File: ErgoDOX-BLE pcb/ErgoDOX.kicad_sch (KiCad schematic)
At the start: 116 parts, among them J1 Conn_01x04, J2 Conn_01x02_Female, J4 Conn_01x02, J5 Conn_01x02, J6 6PIN, P1 USB_C_Plug_USB2.0, Q1 Q_NPN_BCE, SW0:10 SW0:3, SW0:11 SW0:2, SW0:12 SW0:1, SW0:7 SW0:6, SW0:8 SW0:5, SW0:9 SW0:4, SW1:10 SW1:3, SW1:11 SW1:2, SW1:12 SW1:1, SW1:13 SW1:0, SW1:9 SW1:4, SW2:10 SW2:3, SW2:11 SW2:2, SW2:12 SW2:1, SW2:13 SW2:0, SW2:7 SW2:6, SW2:8 SW2:5, SW2:9 SW2:4, SW3:10 SW3:3, SW3:11 SW3:2, SW3:12 SW3:1, SW3:13 SW3:0, SW3:8 SW3:5, SW3:9 SW3:4, SW4:10 SW4:3, SW4:11 SW4:2, SW4:12 SW4:1, SW4:13 SW4:0, SW4:7 SW4:6, SW4:8 SW4:5, SW4:9 SW4:4, SW5:10 SW5:3, SW5:11 SW5:2, SW5:12 SW5:1, SW5:13 SW5:0, SW5:7 SW5:6, SW5:8 SW5:5, SW5:9 SW5:4, U1 MCP23018, U2 MCP73831-2-OT, U3 SPX3819M5-L-3-3

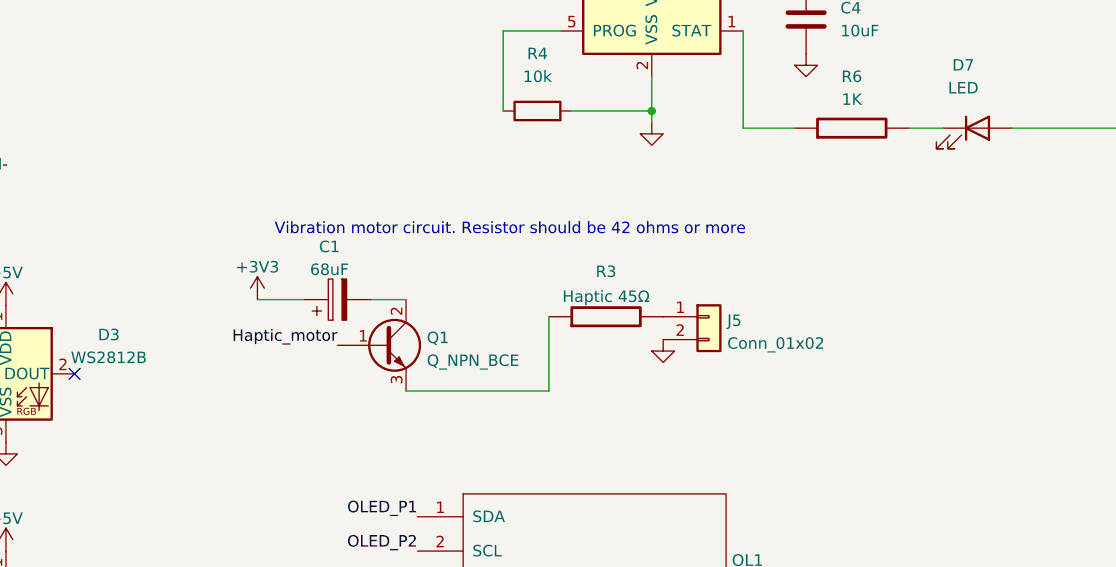
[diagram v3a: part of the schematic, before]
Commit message: Fixing some silk and moving components
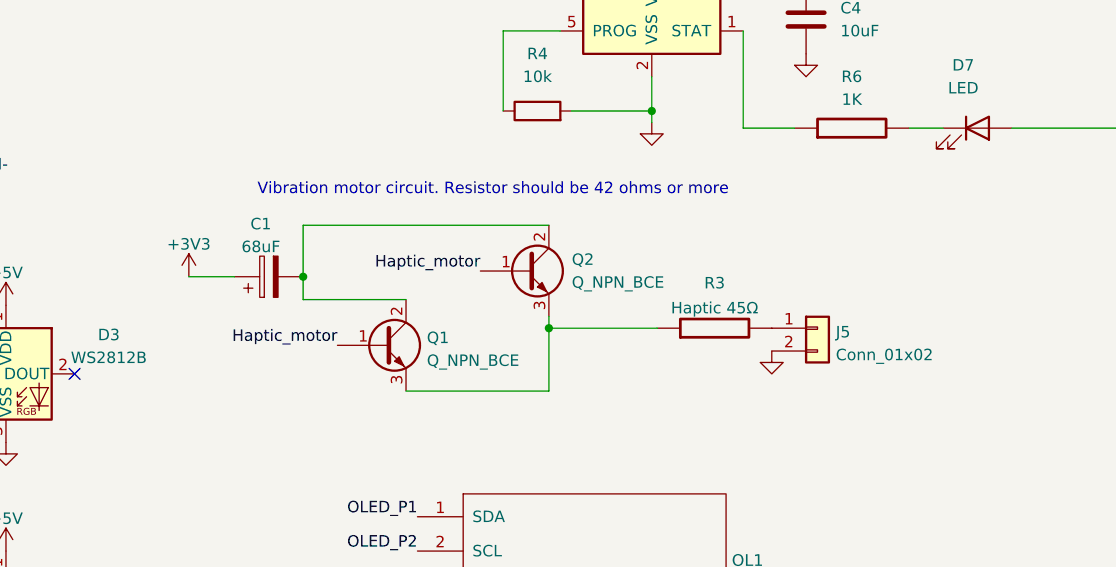
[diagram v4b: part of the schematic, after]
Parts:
- added Q2: Q_NPN_BCE, Package_TO_SOT_SMD:SOT-23, symbol Device:Q_NPN_BCE
- Q1: manf# (none) -> MMBT4401-TP
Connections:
- net Haptic_motor: now also Q2.1 (B)
- net at C1.2, Q1.2 (C): now also Q2.2 (C)
- net at Q1.3 (E), R3.1: now also Q2.3 (E)
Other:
- moved on the sheet: C1, J5, R3
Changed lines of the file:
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@@
   (junction (at 58.42 229.87) (diameter 0) (color 0 0 0 0)
   )
+  (junction (at 302.895 186.055) (diameter 0) (color 0 0 0 0)
+  )
   (junction (at 132.08 238.76) (diameter 0) (color 0 0 0 0)
   )
@@
   (junction (at 96.52 222.25) (diameter 0) (color 0 0 0 0)
   )
+  (junction (at 330.2 191.77) (diameter 0) (color 0 0 0 0)
+  )
   (junction (at 111.76 213.36) (diameter 0) (color 0 0 0 0)
   )
@@
     (stroke (width 0) (type default) (color 0 0 0 0))
   )
-  (wire (pts (xy 330.2 198.755) (xy 330.2 190.5))
+  (wire (pts (xy 330.2 198.755) (xy 330.2 191.77))
     (stroke (width 0) (type default) (color 0 0 0 0))
   )
@@
     (stroke (width 0) (type default) (color 0 0 0 0))
   )
+  (wire (pts (xy 330.2 191.77) (xy 330.2 190.5))
+    (stroke (width 0) (type default) (color 0 0 0 0))
+  )
   (wire (pts (xy 93.98 147.32) (xy 111.76 147.32))
     (stroke (width 0) (type default) (color 0 0 0 0))
@@
     (stroke (width 0) (type default) (color 0 0 0 0))
   )
+  (wire (pts (xy 330.2 191.77) (xy 342.265 191.77))
+    (stroke (width 0) (type default) (color 0 0 0 0))
+  )
   (wire (pts (xy 93.98 229.87) (xy 93.98 234.95))
     (stroke (width 0) (type default) (color 0 0 0 0))
@@
     (stroke (width 0) (type default) (color 0 0 0 0))
   )
-  (wire (pts (xy 297.815 188.595) (xy 302.895 188.595))
+  (wire (pts (xy 290.195 186.055) (xy 295.275 186.055))
     (stroke (width 0) (type default) (color 0 0 0 0))
   )
@@
     (stroke (width 0) (type default) (color 0 0 0 0))
   )
-  (wire (pts (xy 310.515 188.595) (xy 314.325 188.595))
+  (wire (pts (xy 302.895 188.595) (xy 314.325 188.595))
     (stroke (width 0) (type default) (color 0 0 0 0))
   )
@@
     (stroke (width 0) (type default) (color 0 0 0 0))
   )
+  (wire (pts (xy 302.895 180.34) (xy 330.2 180.34))
+    (stroke (width 0) (type default) (color 0 0 0 0))
+  )
   (wire (pts (xy 58.42 180.34) (xy 76.2 180.34))
     (stroke (width 0) (type default) (color 0 0 0 0))
@@
     (stroke (width 0) (type default) (color 0 0 0 0))
   )
+  (wire (pts (xy 302.895 186.055) (xy 302.895 180.34))
+    (stroke (width 0) (type default) (color 0 0 0 0))
+  )
   (wire (pts (xy 93.98 50.8) (xy 93.98 72.39))
     (stroke (width 0) (type default) (color 0 0 0 0))
@@
     (stroke (width 0) (type default) (color 0 0 0 0))
   )
+  (wire (pts (xy 302.895 188.595) (xy 302.895 186.055))
+    (stroke (width 0) (type default) (color 0 0 0 0))
+  )
   (wire (pts (xy 341.63 146.05) (xy 341.63 148.59))
     (stroke (width 0) (type default) (color 0 0 0 0))
@@
   )
   (text "Vibration motor circuit. Resistor should be 42 ohms or more"
-    (at 299.72 181.61 0)
+    (at 297.815 177.165 0)
     (effects (font (size 1.27 1.27)) (justify left bottom))
   )
@@
     (effects (font (size 1.27 1.27)) (justify right bottom))
   )
+  (label "Haptic_motor" (at 322.58 185.42 180)
+    (effects (font (size 1.27 1.27)) (justify right bottom))
+  )
   (label "D_IN_RIGHT+" (at 47.625 100.965 0)
     (effects (font (size 1.27 1.27)) (justify left bottom))
@@
     (pin "1")
   )
-  (symbol (lib_id "Device:C_Polarized") (at 306.705 188.595 90) (unit 1)
+  (symbol (lib_id "Device:C_Polarized") (at 299.085 186.055 90) (unit 1)
     (in_bom yes) (on_board yes) (fields_autoplaced)
-    (property "Reference" "C1" (id 0) (at 305.816 182.7362 90))
-    (property "Value" "68uF" (id 1) (at 305.816 185.2731 90))
-    (property "Footprint" "Capacitor_THT:CP_Radial_Tantal_D5.0mm_P5.00mm" (id 2) (at 310.515 187.6298 0)
+    (property "Reference" "C1" (id 0) (at 298.196 180.1962 90))
+    (property "Value" "68uF" (id 1) (at 298.196 182.7331 90))
+    (property "Footprint" "Capacitor_THT:CP_Radial_Tantal_D5.0mm_P5.00mm" (id 2) (at 302.895 185.0898 0)
       (effects (font (size 1.27 1.27)) hide)
     )
-    (property "Datasheet" "~" (id 3) (at 306.705 188.595 0)
+    (property "Datasheet" "~" (id 3) (at 299.085 186.055 0)
       (effects (font (size 1.27 1.27)) hide)
     )
@@
       (effects (font (size 1.27 1.27)) hide)
     )
+    (property "manf#" "MMBT4401-TP" (id 4) (at 311.785 193.675 0)
+      (effects (font (size 0 0)) hide)
+    )
     (pin "1")
     (pin "2")
@@
     (pin "1")
   )
+  (symbol (lib_id "Device:Q_NPN_BCE") (at 327.66 185.42 0) (unit 1)
+    (in_bom yes) (on_board yes) (fields_autoplaced)
+    (property "Reference" "Q2" (id 0) (at 332.74 184.1499 0)
+      (effects (font (size 1.27 1.27)) (justify left))
+    )
+    (property "Value" "Q_NPN_BCE" (id 1) (at 332.74 186.6899 0)
+      (effects (font (size 1.27 1.27)) (justify left))
+    )
+    (property "Footprint" "Package_TO_SOT_SMD:SOT-23" (id 2) (at 332.74 182.88 0)
+      (effects (font (size 1.27 1.27)) hide)
+    )
+    (property "Datasheet" "~" (id 3) (at 327.66 185.42 0)
+      (effects (font (size 1.27 1.27)) hide)
+    )
+    (property "manf#" "MMBT4401-TP" (id 4) (at 327.66 185.42 0)
+      (effects (font (size 1.27 1.27)) hide)
+    )
+    (pin "1")
+    (pin "2")
+    (pin "3")
+  )
   (symbol (lib_id "component:GND") (at 313.055 247.65 90) (unit 1)
     (in_bom yes) (on_board yes) (fields_autoplaced)
@@
     (pin "1")
   )
-  (symbol (lib_id "component:GND") (at 342.9 194.31 0) (unit 1)
+  (symbol (lib_id "component:GND") (at 354.965 195.58 0) (unit 1)
     (in_bom yes) (on_board yes) (fields_autoplaced)
-    (property "Reference" "#PWR032" (id 0) (at 342.9 194.31 0)
+    (property "Reference" "#PWR032" (id 0) (at 354.965 195.58 0)
       (effects (font (size 0.762 0.762)) hide)
     )
-    (property "Value" "GND" (id 1) (at 342.9 196.088 0)
+    (property "Value" "GND" (id 1) (at 354.965 197.358 0)
       (effects (font (size 0.762 0.762)) hide)
     )
-    (property "Footprint" "" (id 2) (at 342.9 194.31 0)
+    (property "Footprint" "" (id 2) (at 354.965 195.58 0)
       (effects (font (size 1.27 1.27)) hide)
     )
-    (property "Datasheet" "" (id 3) (at 342.9 194.31 0)
+    (property "Datasheet" "" (id 3) (at 354.965 195.58 0)
       (effects (font (size 1.27 1.27)) hide)
     )
@@
     (pin "4")
   )
-  (symbol (lib_id "power:+3V3") (at 297.815 188.595 0) (unit 1)
+  (symbol (lib_id "power:+3V3") (at 290.195 186.055 0) (unit 1)
     (in_bom yes) (on_board yes) (fields_autoplaced)
-    (property "Reference" "#PWR017" (id 0) (at 297.815 192.405 0)
+    (property "Reference" "#PWR017" (id 0) (at 290.195 189.865 0)
       (effects (font (size 1.27 1.27)) hide)
     )
-    (property "Value" "+3V3" (id 1) (at 297.815 184.9905 0))
-    (property "Footprint" "" (id 2) (at 297.815 188.595 0)
+    (property "Value" "+3V3" (id 1) (at 290.195 182.4505 0))
+    (property "Footprint" "" (id 2) (at 290.195 186.055 0)
       (effects (font (size 1.27 1.27)) hide)
     )
-    (property "Datasheet" "" (id 3) (at 297.815 188.595 0)
+    (property "Datasheet" "" (id 3) (at 290.195 186.055 0)
       (effects (font (size 1.27 1.27)) hide)
     )
@@
     (pin "6")
   )
-  (symbol (lib_id "Connector_Generic:Conn_01x02") (at 347.98 190.5 0) (unit 1)
+  (symbol (lib_id "Connector_Generic:Conn_01x02") (at 360.045 191.77 0) (unit 1)
     (in_bom yes) (on_board yes) (fields_autoplaced)
-    (property "Reference" "J5" (id 0) (at 350.012 190.9353 0)
+    (property "Reference" "J5" (id 0) (at 362.077 192.2053 0)
       (effects (font (size 1.27 1.27)) (justify left))
     )
-    (property "Value" "Conn_01x02" (id 1) (at 350.012 193.4722 0)
+    (property "Value" "Conn_01x02" (id 1) (at 362.077 194.7422 0)
       (effects (font (size 1.27 1.27)) (justify left))
     )
-    (property "Footprint" "Connector_PinHeader_2.00mm:PinHeader_1x02_P2.00mm_Vertical" (id 2) (at 347.98 190.5 0)
+    (property "Footprint" "Connector_PinHeader_2.00mm:PinHeader_1x02_P2.00mm_Vertical" (id 2) (at 360.045 191.77 0)
       (effects (font (size 1.27 1.27)) hide)
     )
-    (property "Datasheet" "~" (id 3) (at 347.98 190.5 0)
+    (property "Datasheet" "~" (id 3) (at 360.045 191.77 0)
       (effects (font (size 1.27 1.27)) hide)
     )
-    (property "manf#" "316040001" (id 4) (at 347.98 190.5 0)
+    (property "manf#" "316040001" (id 4) (at 360.045 191.77 0)
       (effects (font (size 1.27 1.27)) hide)
     )
@@
     (pin "9")
   )
-  (symbol (lib_id "component:RESISTOR") (at 336.55 190.5 90) (unit 1)
+  (symbol (lib_id "component:RESISTOR") (at 348.615 191.77 90) (unit 1)
     (in_bom yes) (on_board yes) (fields_autoplaced)
-    (property "Reference" "R3" (id 0) (at 336.55 185.4921 90))
-    (property "Value" "Haptic 45Ω" (id 1) (at 336.55 188.2672 90))
-    (property "Footprint" "ErgoDOX pcb:RESISTOR" (id 2) (at 336.55 190.5 0)
+    (property "Reference" "R3" (id 0) (at 348.615 186.7621 90))
+    (property "Value" "Haptic 45Ω" (id 1) (at 348.615 189.5372 90))
+    (property "Footprint" "ErgoDOX pcb:RESISTOR" (id 2) (at 348.615 191.77 0)
       (effects (font (size 1.27 1.27)) hide)
     )
-    (property "Datasheet" "" (id 3) (at 336.55 190.5 0)
+    (property "Datasheet" "" (id 3) (at 348.615 191.77 0)
       (effects (font (size 1.27 1.27)) hide)
     )
@@
       (reference "Q1") (unit 1) (value "Q_NPN_BCE") (footprint "Package_TO_SOT_SMD:SOT-23")
     )
+    (path "/4bd437c0-b5a5-45dd-be08-807347de90f9"
+      (reference "Q2") (unit 1) (value "Q_NPN_BCE") (footprint "Package_TO_SOT_SMD:SOT-23")
+    )
     (path "/00000000-0000-0000-0000-00004fd9dd65"

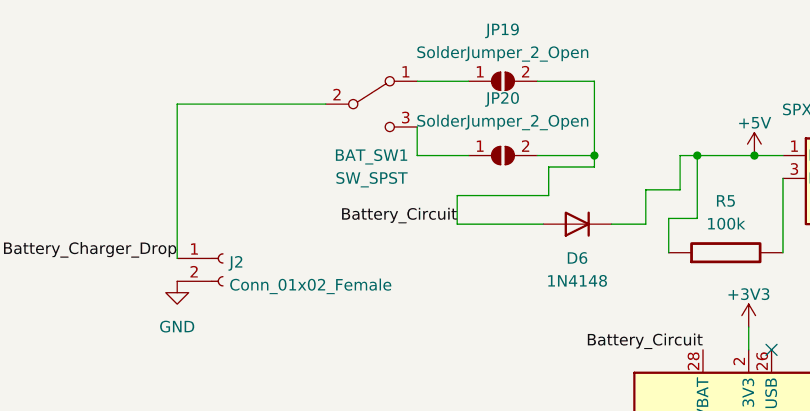
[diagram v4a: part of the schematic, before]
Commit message: Update footprints based on PCB
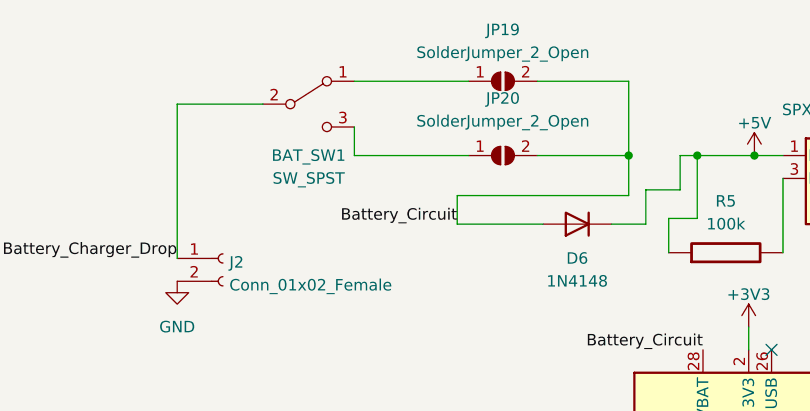
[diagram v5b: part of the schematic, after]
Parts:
- C5: footprint Capacitor_SMD:C_0805_2012Metric_Pad1.18x1.45mm_HandSolder -> Capacitor_SMD:C_0805_2012Metric
- D1:7, D1:8: footprint (none) -> DIODE
- LED_A1, LED_B1, LED_C1: footprint (none) -> MX_LED
- S1, S2: footprint (none) -> STAB_PCB940
- SX0:10, SX0:11, SX1:7, SX1:8: footprint (none) -> MX_FLIP
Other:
- moved on the sheet: BAT_SW1

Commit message: Add some data sheets and model numbers
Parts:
- C2: footprint Capacitor_THT:C_Disc_D3.8mm_W2.6mm_P2.50mm -> Capacitor_SMD:C_0805_2012Metric; manf# (none) -> CC0805ZKY5V6BB106
- SW_RST1: manf# (none) -> TL1105VF250Q
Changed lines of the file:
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@@
       (effects (font (size 1.524 1.524)) hide)
     )
-    (property "Datasheet" "" (id 3) (at 73.66 21.59 0)
+    (property "Datasheet" "https://sten-eswitch-13110800-production.s3.amazonaws.com/system/asset/product_line/data_sheet/144/TL1105.pdf" (id 3) (at 73.66 21.59 0)
       (effects (font (size 1.524 1.524)) hide)
+    )
+    (property "manf#" "TL1105VF250Q" (id 4) (at 73.66 21.59 0)
+      (effects (font (size 1.27 1.27)) hide)
     )
     (pin "1")
@@
       (effects (font (size 1.27 1.27)) hide)
     )
-    (property "Datasheet" "" (id 3) (at 363.855 169.545 0)
+    (property "Datasheet" "https://www.yageo.com/upload/media/product/productsearch/datasheet/rchip/PYu-RC_Group_51_RoHS_L_12.pdf" (id 3) (at 363.855 169.545 0)
       (effects (font (size 1.27 1.27)) hide)
     )
@@
       (effects (font (size 1.27 1.27)) hide)
     )
-    (property "Datasheet" "" (id 3) (at 254 37.465 0)
+    (property "Datasheet" "https://www.seielect.com/Catalog/SEI-RNCF.pdf" (id 3) (at 254 37.465 0)
       (effects (font (size 1.27 1.27)) hide)
     )
@@
     )
     (property "Datasheet" "~" (id 3) (at 188.595 223.52 0)
-      (effects (font (size 1.27 1.27)) hide)
-    )
-    (pin "1")
-    (pin "2")
-  )
-  (symbol (lib_id "Device:C") (at 198.12 73.66 0) (unit 1)
-    (in_bom yes) (on_board yes) (fields_autoplaced)
-    (property "Reference" "C2" (id 0) (at 201.93 72.3899 0)
-      (effects (font (size 1.27 1.27)) (justify left))
-    )
-    (property "Value" "10uF" (id 1) (at 201.93 74.9299 0)
-      (effects (font (size 1.27 1.27)) (justify left))
-    )
-    (property "Footprint" "Capacitor_THT:C_Disc_D3.8mm_W2.6mm_P2.50mm" (id 2) (at 199.0852 77.47 0)
-      (effects (font (size 1.27 1.27)) hide)
-    )
-    (property "Datasheet" "~" (id 3) (at 198.12 73.66 0)
       (effects (font (size 1.27 1.27)) hide)
     )
@@
       (effects (font (size 1.27 1.27)) hide)
     )
-    (property "Datasheet" "https://assets.nexperia.com/documents/data-sheet/1N4148_1N4448.pdf" (id 3) (at 237.49 34.29 0)
+    (property "Datasheet" "~" (id 3) (at 237.49 34.29 0)
       (effects (font (size 1.27 1.27)) hide)
     )
@@
     (pin "5")
   )
+  (symbol (lib_id "Device:C") (at 198.12 73.66 0) (unit 1)
+    (in_bom yes) (on_board yes) (fields_autoplaced)
+    (property "Reference" "C2" (id 0) (at 201.93 72.3899 0)
+      (effects (font (size 1.27 1.27)) (justify left))
+    )
+    (property "Value" "10uF" (id 1) (at 201.93 74.9299 0)
+      (effects (font (size 1.27 1.27)) (justify left))
+    )
+    (property "Footprint" "Capacitor_SMD:C_0805_2012Metric" (id 2) (at 199.0852 77.47 0)
+      (effects (font (size 1.27 1.27)) hide)
+    )
+    (property "Datasheet" "https://www.yageo.com/upload/media/product/productsearch/datasheet/mlcc/UPY-GPHC_Y5V_6.3V-to-50V_11.pdf" (id 3) (at 198.12 73.66 0)
+      (effects (font (size 1.27 1.27)) hide)
+    )
+    (property "manf#" "CC0805ZKY5V6BB106" (id 4) (at 198.12 73.66 0)
+      (effects (font (size 1.27 1.27)) hide)
+    )
+    (pin "1")
+    (pin "2")
+  )
   (symbol (lib_id "Connector:Conn_01x02_Female") (at 198.12 38.1 0) (unit 1)
     (in_bom yes) (on_board yes) (fields_autoplaced)
@@
       (reference "C1") (unit 1) (value "68uF") (footprint "Capacitor_THT:CP_Radial_Tantal_D5.0mm_P5.00mm")
     )
-    (path "/a0eea18c-fd7a-428a-808b-290b4bd06294"
-      (reference "C2") (unit 1) (value "10uF") (footprint "Capacitor_THT:C_Disc_D3.8mm_W2.6mm_P2.50mm")
+    (path "/f6842c47-ad13-444d-a937-7b853dfac944"
+      (reference "C2") (unit 1) (value "10uF") (footprint "Capacitor_SMD:C_0805_2012Metric")
     )
     (path "/5573bfb7-1fbc-4713-8b3e-20d1545510fe"

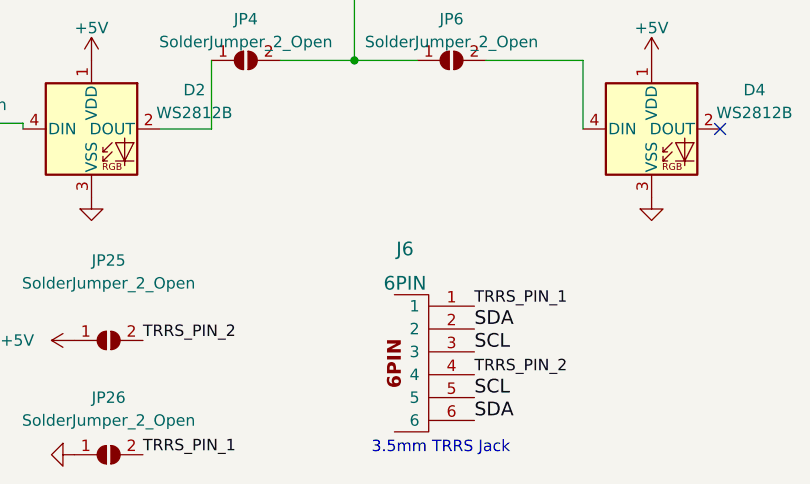
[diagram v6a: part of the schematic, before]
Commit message: Silkscreen cleanup
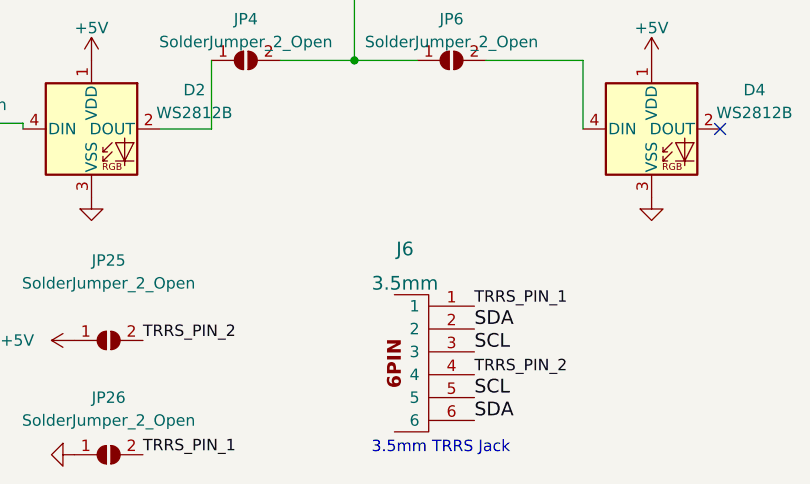
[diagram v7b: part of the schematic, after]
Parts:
- J6: value 6PIN -> 3.5mm
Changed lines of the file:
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@@
       (effects (font (size 1.524 1.524)))
     )
-    (property "Value" "6PIN" (id 1) (at 242.4773 241.3 0)
+    (property "Value" "3.5mm" (id 1) (at 242.4773 241.3 0)
       (effects (font (size 1.524 1.524)))
     )
@@
     )
     (path "/bea7f2ce-f656-49f6-aed6-635d4b2b3bb7"
-      (reference "J6") (unit 1) (value "6PIN") (footprint "ErgoDOX pcb:4pin35mmAudio")
+      (reference "J6") (unit 1) (value "3.5mm") (footprint "ErgoDOX pcb:4pin35mmAudio")
     )
     (path "/131c2f34-19ec-4ccc-8120-2b0363648606"

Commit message: Start adding notes for corrections
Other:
- note added: "TODO: All PADs for Kalih hotswaps need to be opposite side Holes for Kalih hotswaps need to be a tiny bit smaller Add notes for the Battery connector: it is easy to put it on with the wrong polarity"
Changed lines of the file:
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@@
+    (effects (font (size 1.27 1.27)) (justify left bottom))
+  )
+  (text "TODO:\nAll PADs for Kalih hotswaps need to be opposite side\nHoles for Kalih hotswaps need to be a tiny bit smaller\nAdd notes for the Battery connector: it is easy to put it on with the wrong polarity"
+    (at 344.805 23.495 0)
     (effects (font (size 1.27 1.27)) (justify left bottom))
   )
